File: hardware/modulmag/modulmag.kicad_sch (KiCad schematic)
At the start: 0 parts

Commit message: Hardver: modulmag + vezérlő kapcsolási rajz (vázlat, ERC tiszta)
Elektromosan a MODULMAG-SPEC és a VEZERLO-SPEC szerint, elrendezés nélkül.
Közös könyvtár: saját szimbólumok, ESP32-C6-WROOM-1/-1U footprint (Espressif,
CC-BY-SA, licenc a lib/-ben). A KiCad .history/ mappája gitignore-ba.

Co-Authored-By: Claude Opus 5.5 <noreply@anthropic.com>
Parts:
- added C1: 10µ/50V, Capacitor_SMD:C_1210_3225Metric, symbol Device:C
- added C10, C11: 12p, Capacitor_SMD:C_0603_1608Metric, symbol Device:C
- added C12: 47µ/50V, Capacitor_SMD:CP_Elec_6.3x7.7, symbol Device:C_Polarized
- added C13, C19: 4µ7, Capacitor_SMD:C_0603_1608Metric, symbol Device:C
- added C14: 1µ, Capacitor_SMD:C_0603_1608Metric, symbol Device:C
- added C15: 10n, Capacitor_SMD:C_0603_1608Metric, symbol Device:C
- added C16, C17, C18, C4, C5, C6, C7, C8, C9: 100n, Capacitor_SMD:C_0603_1608Metric, symbol Device:C
- added C2: 22µ/10V, Capacitor_SMD:C_1206_3216Metric, symbol Device:C
- added C3: 10µ tantál, Capacitor_Tantalum_SMD:CP_EIA-3216-18_Kemet-A, symbol Device:C_Polarized
- added D1: SS16, Diode_SMD:D_SMA, symbol Device:D_Schottky
- added D2: SMBJ28A, Diode_SMD:D_SMB, symbol Device:D_Zener
- added D3: zöld, LED_SMD:LED_0603_1608Metric, symbol Device:LED
- added D4: piros, LED_SMD:LED_0603_1608Metric, symbol Device:LED
- added D5: SMF5.0A, Diode_SMD:D_SOD-123F, symbol Device:D_Zener
- added F1: 0,5A, Fuse:Fuse_1206_3216Metric, symbol Device:Fuse
- added F2: PTC 0,5A, Fuse:Fuse_1206_3216Metric, symbol Device:Polyfuse
- added FB1: ferrit ≤0,1Ω, Inductor_SMD:L_0603_1608Metric, symbol Device:FerriteBead_Small
- added J1: DEBUG, Connector_PinHeader_2.54mm:PinHeader_1x07_P2.54mm_Vertical, symbol Connector_Generic:Conn_01x07
- added J2: BUS_IN, Connector_JST:JST_XH_B4B-XH-A_1x04_P2.50mm_Vertical, symbol Connector_Generic:Conn_01x04
- added J3: BUS_OUT, Connector_JST:JST_XH_B4B-XH-A_1x04_P2.50mm_Vertical, symbol Connector_Generic:Conn_01x04
- added JP1: LEZÁRÁS, Connector_PinHeader_2.54mm:PinHeader_1x02_P2.54mm_Vertical, symbol Jumper:Jumper_2_Open
- added R1, R2, R4: 10k, Resistor_SMD:R_0603_1608Metric, symbol Device:R
- added R3: 150k, Resistor_SMD:R_0603_1608Metric, symbol Device:R
- added R5: 120R, Resistor_SMD:R_0805_2012Metric, symbol Device:R
- added R6: 10R, Resistor_SMD:R_1206_3216Metric, symbol Device:R
- added R8: 2k2, Resistor_SMD:R_0603_1608Metric, symbol Device:R
- added R9: 1k, Resistor_SMD:R_0603_1608Metric, symbol Device:R
- added TP1: BOOT0, TestPoint:TestPoint_Pad_D1.5mm, symbol Connector:TestPoint
- added TP2: 3V3, TestPoint:TestPoint_Pad_D1.5mm, symbol Connector:TestPoint
- added U1: P78E05-1000, Converter_DCDC:Converter_DCDC_RECOM_R-78E-0.5_THT, symbol Converter_DCDC:R-78E5.0-1.0
- added U2: ISO1042BDWV, Package_SO:SOIC-8_7.5x5.85mm_P1.27mm, symbol modularis:ISO1042BDWV
- added U3: ESD2CAN24-Q1, Package_TO_SOT_SMD:SOT-23, symbol Power_Protection:NUP2105L
- added U5: NCP1117ST33T3G, Package_TO_SOT_SMD:SOT-223-3_TabPin2, symbol Regulator_Linear:NCP1117-3.3_SOT223
- added U6: STM32F303RET6, Package_QFP:LQFP-64_10x10mm_P0.5mm, symbol MCU_ST_STM32F3:STM32F303RETx
- added Y1: 8MHz, Crystal:Crystal_SMD_3225-4Pin_3.2x2.5mm, symbol Device:Crystal_GND24
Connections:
- new net +24V_D1: D1.1 (K), R6.1
- new net +24V_F1: D1.2 (A), F1.2
- new net +24V_IN: F1.1
- new net +24V_P: C1.1, C12.1, D2.1 (K), R3.1, R6.2, U1.1 (IN)
- new net +3V3: C13.1, C17.1, C3.1, C4.1, C5.1, C6.1, C7.1, C8.1, FB1.1, J1.1 (Pin_1), R1.1, R8.1, R9.1, TP2.1, U2.1 (VCC1), U5.2 (VO), U6.1 (VBAT), U6.19 (VDD), U6.32 (VDD), U6.48 (VDD), U6.64 (VDD)
- new net +3V3A: C14.1, C15.1, FB1.2, U6.13 (VDDA)
- new net +5V: C2.1, U1.3 (OUT), U5.3 (VI)
- new net BOOT0: R2.1, TP1.1, U6.60 (BOOT0)
- new net CAN_H: J2.4 (Pin_4), J3.4 (Pin_4), JP1.1 (A), U2.7 (CANH), U3.2 (K)
- new net CAN_L: J2.3 (Pin_3), J3.3 (Pin_3), R5.2, U2.6 (CANL), U3.1 (K)
- new net CAN_RX: U2.3 (RXD), U6.44 (PA11)
- new net CAN_TERM: JP1.2 (B), R5.1
- new net CAN_TX: R1.2, U2.2 (TXD), U6.45 (PA12)
- new net GND: C1.2, C10.2, C11.2, C12.2, C13.2, C14.2, C15.2, C16.2, C17.2, C2.2, C3.2, C4.2, C5.2, C6.2, C7.2, C8.2, C9.2, D2.2 (A), D3.1 (K), J1.3 (Pin_3), R2.2, R4.2, U1.2 (GND), U2.4 (GND1), U5.1 (GND), U6.12 (VSSA), U6.18 (VSS), U6.31 (VSS), U6.47 (VSS), U6.63 (VSS), Y1.2 (G), Y1.4 (G)
- new net GND_BUS: C18.2, C19.2, D5.2 (A), J2.2 (Pin_2), J3.2 (Pin_2), U2.5 (GND2), U3.3 (A)
- new net HW_ID: U6.8 (PC0)
- new net LED_PWR: D3.2 (A), R8.2
- new net LED_STAT: D4.2 (A), R9.2
- new net NRST: C16.1, J1.5 (Pin_5), U6.7 (NRST)
- new net OSC_IN: C10.1, U6.5 (PF0), Y1.1
- new net OSC_OUT: C11.1, U6.6 (PF1), Y1.3
- new net PA0: U6.14 (PA0)
- new net PA1: U6.15 (PA1)
- new net PA10: U6.43 (PA10)
- new net PA2: U6.16 (PA2)
- new net PA3: U6.17 (PA3)
- new net PA4: U6.20 (PA4)
- new net PA5: U6.21 (PA5)
- new net PA6: U6.22 (PA6)
- new net PA7: U6.23 (PA7)
- new net PA8: U6.41 (PA8)
- new net PA9: U6.42 (PA9)
- new net PB11: U6.30 (PB11)
- new net PB12: U6.33 (PB12)
- new net PB13: U6.34 (PB13)
- new net PB14: U6.35 (PB14)
- new net PB15: U6.36 (PB15)
- new net PB8: U6.61 (PB8)
- new net PB9: U6.62 (PB9)
- new net PC2: U6.10 (PC2)
- new net PC3: U6.11 (PC3)
- new net PC6: U6.37 (PC6)
- new net PC7: U6.38 (PC7)
- new net PC8: U6.39 (PC8)
- new net STATUS_LED: D4.1 (K), U6.2 (PC13)
- new net SWCLK: J1.2 (Pin_2), U6.49 (PA14)
- new net SWDIO: J1.4 (Pin_4), U6.46 (PA13)
- new net UART_RX: J1.7 (Pin_7), U6.25 (PC5)
- new net UART_TX: J1.6 (Pin_6), U6.24 (PC4)
- new net VIN_SENSE: C9.1, R3.2, R4.1, U6.9 (PC1)
- new net V_BUS: F2.1, J2.1 (Pin_1), J3.1 (Pin_1)
- new net V_BUS_P: C18.1, C19.1, D5.1 (K), F2.2, U2.8 (VCC2)
- no-connect marks 0 -> 17
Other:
- note added: "2. TÁP: +24V_IN → F1 → D1 → R6 → +24V_P → P78E05 (5 V) → NCP1117 (3,3 V) (D56, D57 – a 24 V-os tápot ≤ 26 V-ra!)"
- note added: "3. STM32F303RET6 – a modulspecifikus lábak hierarchikus címkék (a modul lapja köti be vagy köti NC-re)"
- note added: "4. IZOLÁLT CAN – ISO1042BDWV: a tok alatt minden rétegen rézmentes rés"
- note added: "5. BUSZ-OLDAL (GND_BUS-tartomány): J2/J3 azonos tűi átmenők"
- note added: "D55 nyitott: TVS + PTC („legjobb erőfeszítés”) vagy TPS2660 eFuse modulonként"
- note added: "Hidegítés: lábanként 100 nF a saját VDD-lábánál; VDDA a 3V3-ról FB1-en át (nem jöhet fel később, mint a VDD)"
- note added: "J1: 1 VTref · 2 SWCLK · 3 GND · 4 SWDIO · 5 NRST · 6 TX · 7 RX (ST-Link klón dupont-tal)"
- note added: "VIN_SENSE: 24 V → 1,5 V (PC1)"
- note added: "VÁZLAT – generálva a MODULMAG-SPEC.md alapján (2026-10-14). Elrendezést rendezd; a bekötés címkékkel kész."
- title: Modulmag (közös: STM32F303 + izolált CAN + táp) -> Modulmag – STM32F303RET6 + izolált CAN + 24 V → 5 V → 3,3 V

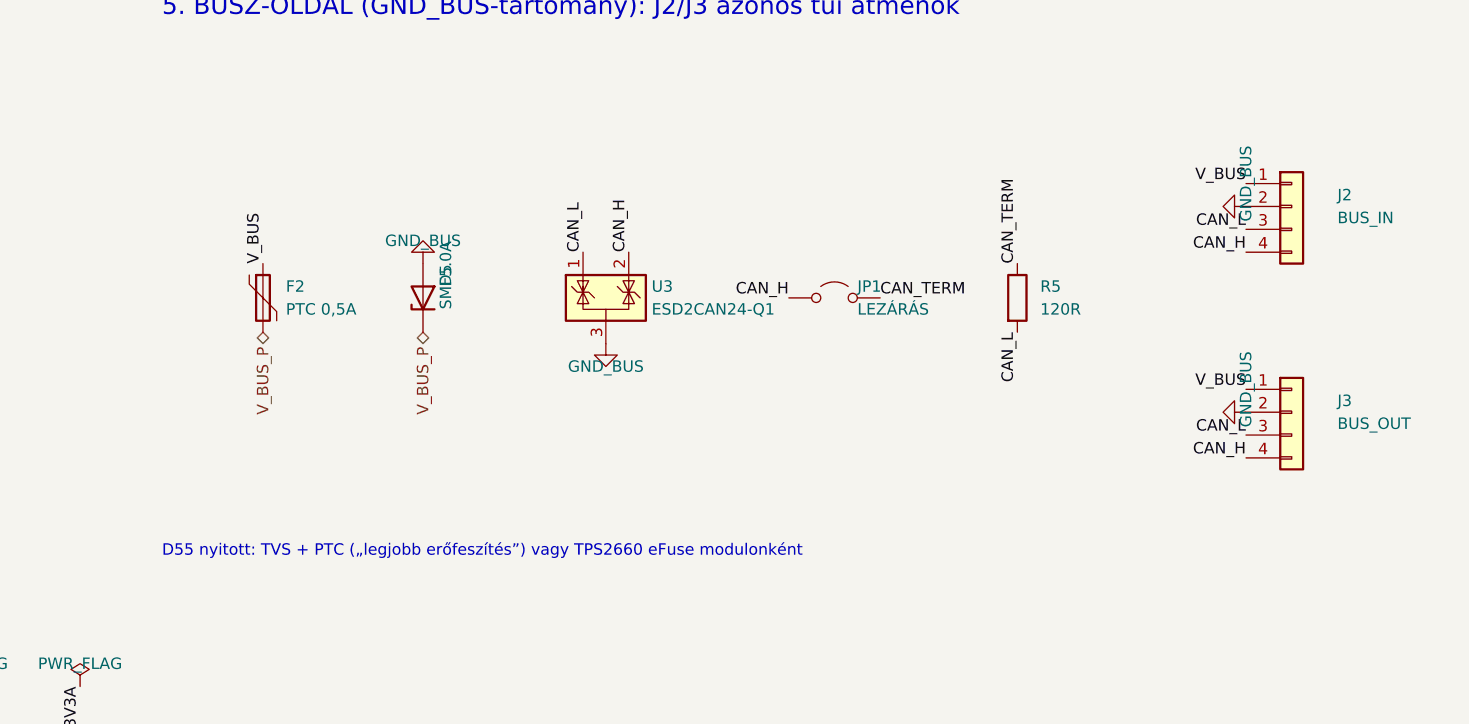
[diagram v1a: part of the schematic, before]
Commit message: Hardver: modulmag – PTC (F2) ki a V_BUS-ról, TVS marad (D55)
A J2/J3 V_BUS-a közvetlenül a V_BUS_P; a D5 TVS az ESD / hot-plug ellen.
A HW-ID osztó továbbra is a modul saját lapján (a modulmag csak HW_ID-t ad).

Co-Authored-By: Claude Opus 5.5 <noreply@anthropic.com>
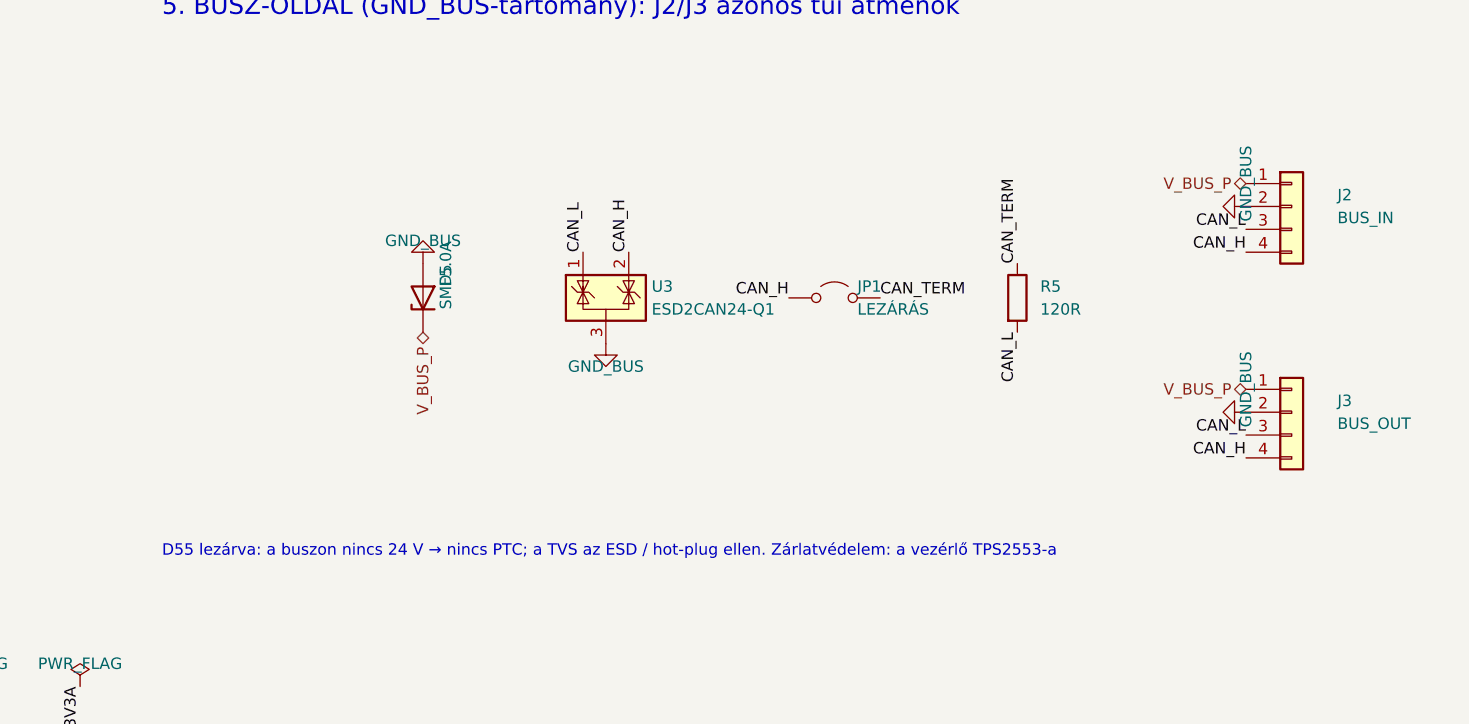
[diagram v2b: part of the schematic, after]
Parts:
- removed F2: PTC 0,5A, Fuse:Fuse_1206_3216Metric, symbol Device:Polyfuse
- D5: Megjegyzés (none) -> ESD / hot-plug tüskék ellen, a J2/J3 mellé
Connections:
- net V_BUS is gone; now on net V_BUS_P: J2.1 (Pin_1), J3.1 (Pin_1)
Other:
- note added: "D55 lezárva: a buszon nincs 24 V → nincs PTC; a TVS az ESD / hot-plug ellen. Zárlatvédelem: a vezérlő TPS2553-a"
- note removed: "D55 nyitott: TVS + PTC („legjobb erőfeszítés”) vagy TPS2660 eFuse modulonként"

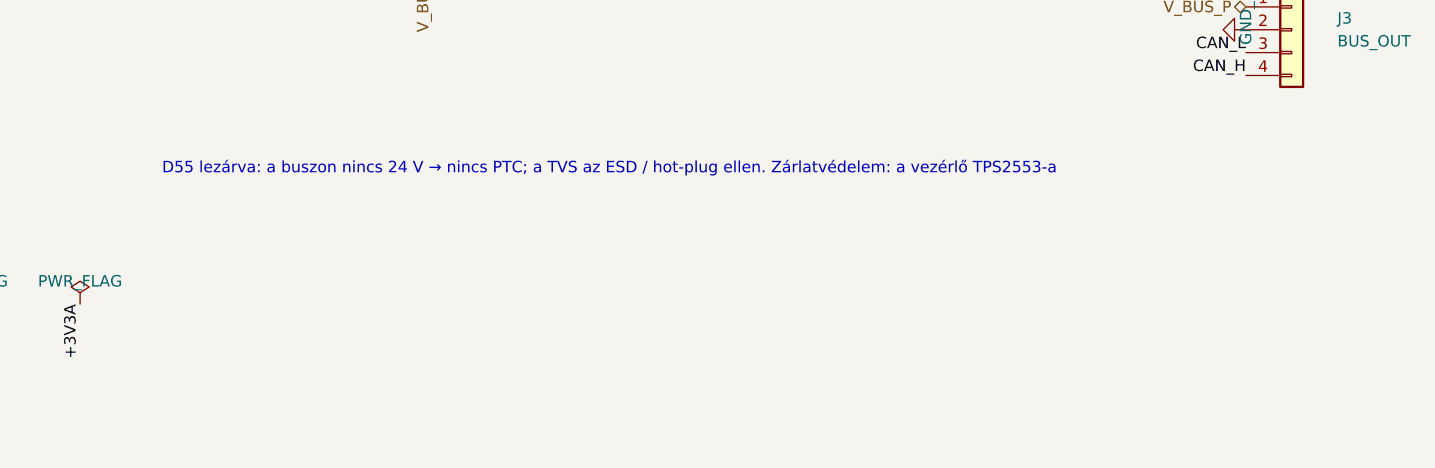
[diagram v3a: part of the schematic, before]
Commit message: Hardver: bemeneti modul kapcsolási rajz + HDC3020 + buszos táp opció
16 bemenet JST-PH-n (1k + 10k felhúzás + 10 nF, osztó-footprint, ESD),
4 érzékelő-tápcsoport (3,3 / 5 V forrasztható választó + PTC, külön NCP1117),
HDC3020 (saját szimbólum + DEF0008A footprint) + külső I²C PH-csatlakozó.
Modulmag: opcionális buszos táp (D6 + JP2, alapból üres) – D66. ERC: 0 hiba.

Co-Authored-By: Claude Opus 5.5 <noreply@anthropic.com>
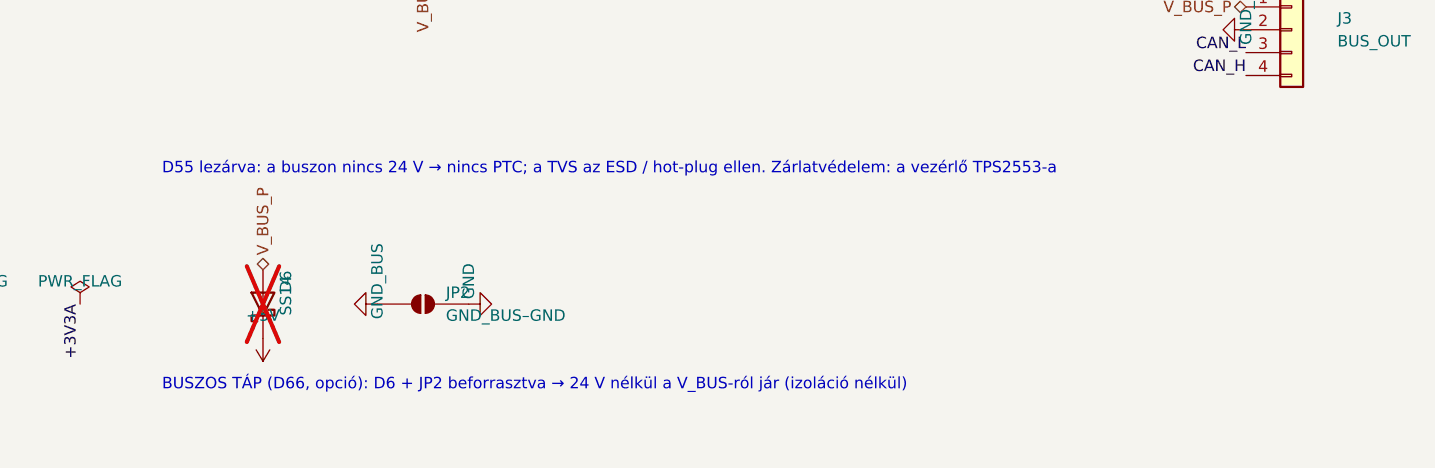
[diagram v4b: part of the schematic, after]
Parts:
- added D6: SS14, Diode_SMD:D_SMA, symbol Device:D_Schottky
- added JP2: GND_BUS–GND, Jumper:SolderJumper-2_P1.3mm_Open_RoundedPad1.0x1.5mm, symbol Jumper:SolderJumper_2_Open
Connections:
- net +5V: now also D6.1 (K)
- net GND: now also JP2.2 (B)
- net GND_BUS: now also JP2.1 (A)
- net V_BUS_P: now also D6.2 (A)
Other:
- note added: "BUSZOS TÁP (D66, opció): D6 + JP2 beforrasztva → 24 V nélkül a V_BUS-ról jár (izoláció nélkül)"

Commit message: Hardver: mind az öt kapcsolási rajz elrendezve (vezetékes, blokkos), netlista-ellenőrzővel
Funkcionális blokkok, balról jobbra jelút, tápsín felül / GND alul; blokkon belül
vezeték, blokkok között és az IC-lábakon címke. kigen: lábpozíció, place(),
wire/junction/rail, tükrözés, 1,27 mm-es rács, olvasható mezők. gen/netcmp.py:
két netlista lábszintű összevetése – a bekötés az átrendezés előttivel azonos
(a modulmag D66-os D6/JP2-jét kivéve). ERC: 0 hiba mind az öt lapon.

Co-Authored-By: Claude Opus 5.5 <noreply@anthropic.com>
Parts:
- D1: Megjegyzés (none) -> fordított polaritás ellen
- D2: Megjegyzés (none) -> TVS, 28 V standoff
- D3: Megjegyzés (none) -> táp-LED
- D4: Megjegyzés (none) -> állapot-LED, a PC13 nyeli
- D6: Megjegyzés DNP – buszos táp: V_BUS → +5V (24 V nélkül); izoláció nélkü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 -> DNP – buszos táp: V_BUS → +5V
- FB1: Megjegyzés (none) -> vagy 0 Ω
- R2: Megjegyzés (none) -> BOOT0 lehúzás – normál indulás a flashből
- TP1: Megjegyzés (none) -> 3V3-ra húzva: ROM-bootloader (USART1)
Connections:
- net +24V_D1: no longer names the net of D1.1 (K), R6.1
- net +24V_F1: no longer names the net of D1.2 (A), F1.2
- net CAN_TERM: no longer names the net of JP1.2 (B), R5.1
- net LED_PWR: no longer names the net of D3.2 (A), R8.2
- net LED_STAT: no longer names the net of D4.2 (A), R9.2
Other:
- note added: "(ST-Link klón dupont-tal; beültetés opcionális)"
- note added: "1. TÁP: +24V_IN → F1 → D1 → R6 → +24V_P → U1 P78E05 (5 V) → U5 NCP1117 (3,3 V)"
- note added: "2. STM32F303RET6 – a modulspecifikus lábak hierarchikus címkék (a modul lapja köti be vagy hagyja üresen)"
- note added: "3. IZOLÁLT CAN – ISO1042BDWV: a tok alatt minden rétegen rézmentes rés"
- note added: "4. BUSZ-OLDAL (GND_BUS): J2 és J3 azonos tűi átmenők; ESD és TVS a csatlakozók mellé"
- note added: "BUSZOS TÁP (D66, opció): D6 + JP2 beforrasztva → 24 V nélkül"
- note added: "D56, D57 – a C12 elkó kötelező; a 24 V-os tápot ≤ 26 V-ra! (a P78E05 max. 36 V)"
- note added: "DEBUG – J1: 1 VTref · 2 SWCLK · 3 GND · 4 SWDIO · 5 NRST · 6 TX · 7 RX"
- note added: "Generálva a MODULMAG-SPEC.md alapján (hardware/gen/modulmag.py) – kézi szerkesztés helyett a generátort módosítsd."
- note added: "HIDEGÍTÉS: lábanként 100 nF a saját VDD-lábánál; VDDA a 3V3-ról FB1-en át"
- note added: "HSE 8 MHz"
- note added: "RESET / BOOT0"
- note added: "TXD felhúzás (bootkor recesszív busz):"
- note added: "V_BUS TVS · CAN ESD · lezárás (JP1: csak a lánc két végén)"
- note added: "a V_BUS-ról jár (izoláció nélkül!)"
- note added: "logikai oldal (GND) busz-oldal (GND_BUS)"
- note added: "ÁLLAPOT-LED-ek (előlap, fényvezető)"
- note removed: "2. TÁP: +24V_IN → F1 → D1 → R6 → +24V_P → P78E05 (5 V) → NCP1117 (3,3 V) (D56, D57 – a 24 V-os tápot ≤ 26 V-ra!)"
- note removed: "3. STM32F303RET6 – a modulspecifikus lábak hierarchikus címkék (a modul lapja köti be vagy köti NC-re)"
- note removed: "4. IZOLÁLT CAN – ISO1042BDWV: a tok alatt minden rétegen rézmentes rés"
- note removed: "5. BUSZ-OLDAL (GND_BUS-tartomány): J2/J3 azonos tűi átmenők"
- note removed: "BUSZOS TÁP (D66, opció): D6 + JP2 beforrasztva → 24 V nélkül a V_BUS-ról jár (izoláció nélkül)"
- note removed: "D55 lezárva: a buszon nincs 24 V → nincs PTC; a TVS az ESD / hot-plug ellen. Zárlatvédelem: a vezérlő TPS2553-a"
- note removed: "Hidegítés: lábanként 100 nF a saját VDD-lábánál; VDDA a 3V3-ról FB1-en át (nem jöhet fel később, mint a VDD)"
- note removed: "J1: 1 VTref · 2 SWCLK · 3 GND · 4 SWDIO · 5 NRST · 6 TX · 7 RX (ST-Link klón dupont-tal)"
- note removed: "VÁZLAT – generálva a MODULMAG-SPEC.md alapján (2026-10-14). Elrendezést rendezd; a bekötés címkékkel kész."
